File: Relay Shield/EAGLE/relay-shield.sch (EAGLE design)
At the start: 47 parts, among them J1 POWER_JACKSLT, Q1 MPSA42, Q2 MPSA42, Q3 MPSA42, Q4 MPSA42, U1 RELAYPANASONIC-JS, U2 RELAYPANASONIC-JS, U3 RELAYPANASONIC-JS, U4 RELAYPANASONIC-JS, U6 LM2672

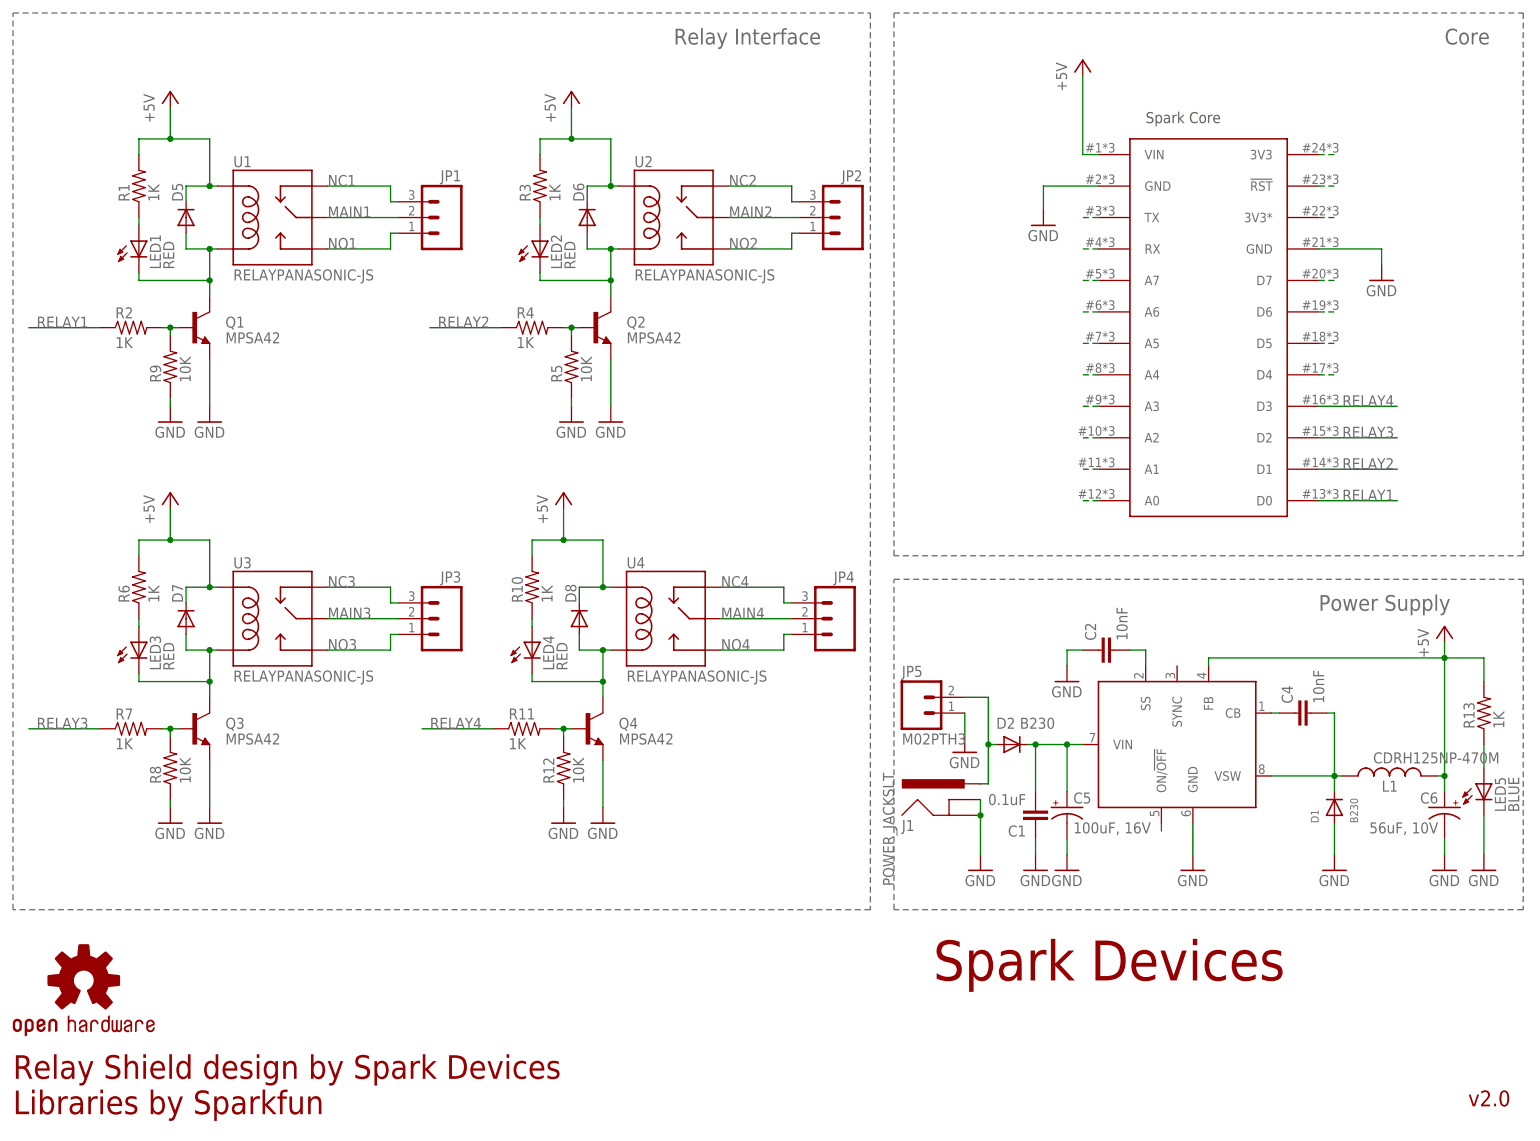
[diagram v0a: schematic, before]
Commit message: updated designators and bom
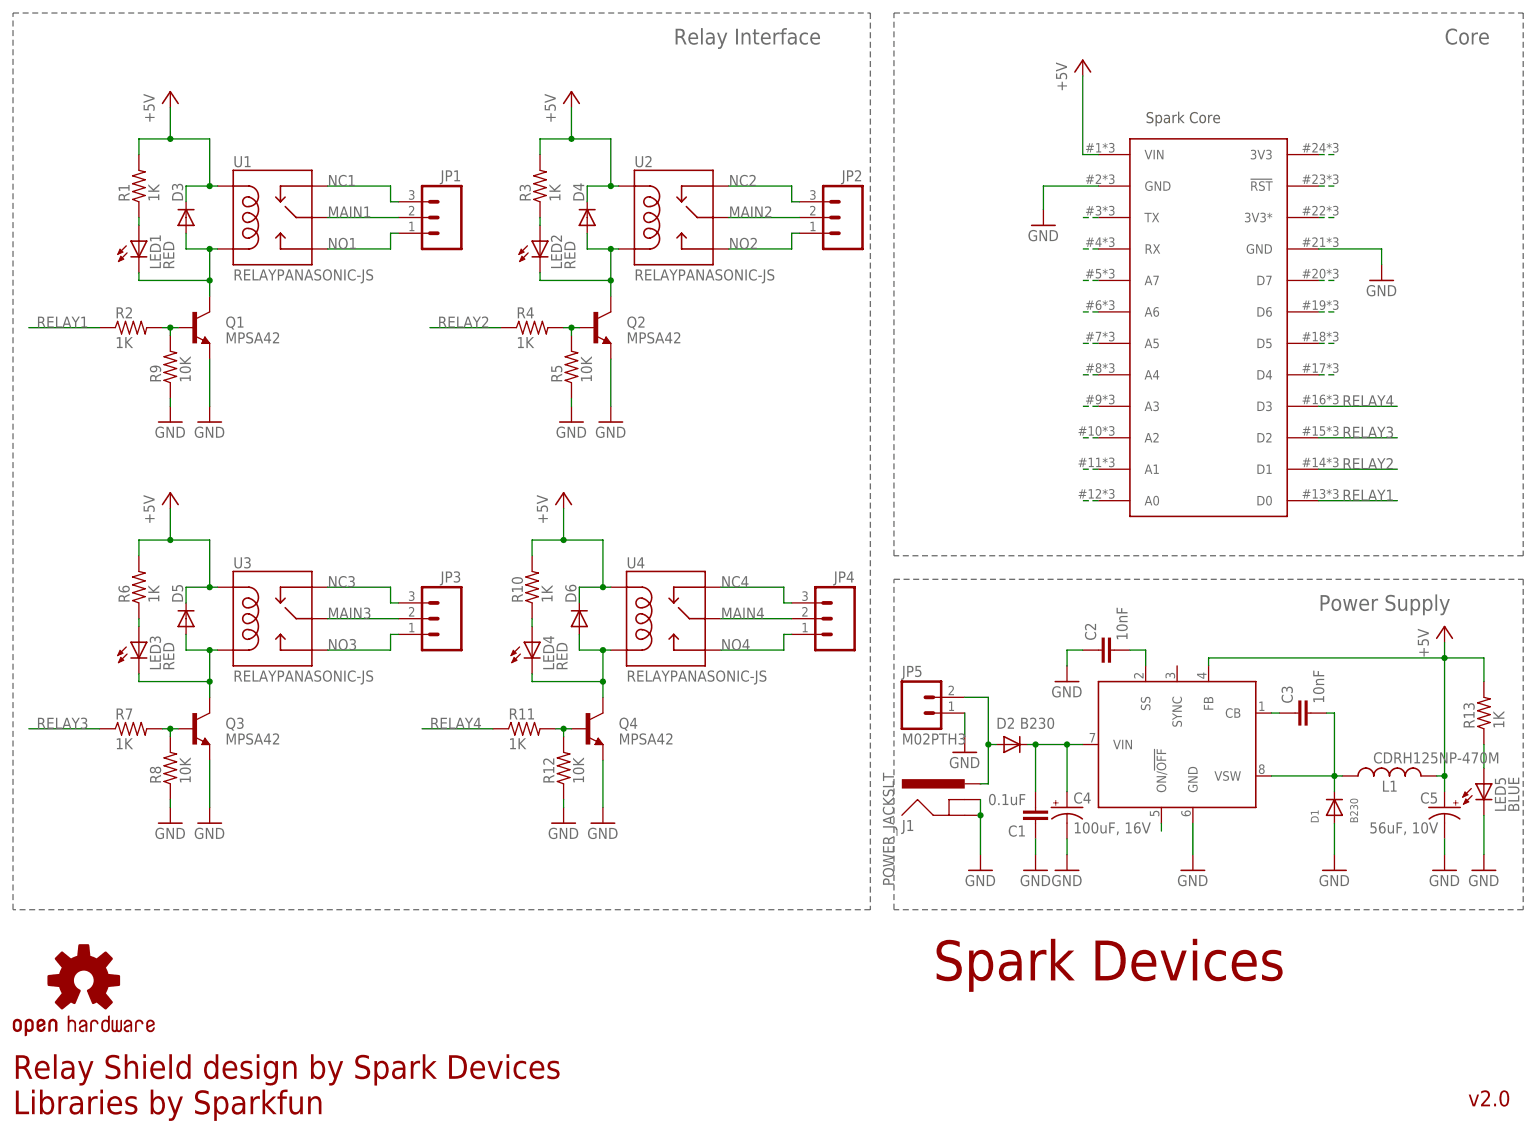
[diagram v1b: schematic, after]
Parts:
- removed C6: 56uF, 10V, SparkFun-Capacitors:CAP_POLD
- removed D7, D8: (no value), diode:DIODE-SOD123
- added C3: 10nF, SparkFun-Capacitors:CAP0603-CAP
- added D3, D4: (no value), diode:DIODE-SOD123
- C4: value 10nF -> 100uF, 16V; device SparkFun-Capacitors:CAP0603-CAP -> SparkFun-Capacitors:CAP_POLD
- C5: value 100uF, 16V -> 56uF, 10V
- renumbered U6 to U5
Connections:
- net +5V: now also C5.+, D3.C, D4.C; no longer C6.+, D7.C, D8.C
- net GND: now also C4.-; no longer C6.-
- net N$1: now also D3.A; no longer D5.A
- net N$11: now also D6.A; no longer D8.A
- net N$14: now also C4.+; no longer C5.+
- net N$33: now also C3.1; no longer C4.1
- net N$34: now also C3.2; no longer C4.2
- net N$5: now also D4.A; no longer D6.A
- net N$8: now also D5.A; no longer D7.A
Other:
- moved on the sheet: C5, D5, D6
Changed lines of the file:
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@@
 <part name="Q3" library="SparkFun-DiscreteSemi" deviceset="TRANSISTOR_NPN" device="MPSA42" value="MPSA42"/>
 <part name="Q4" library="SparkFun-DiscreteSemi" deviceset="TRANSISTOR_NPN" device="MPSA42" value="MPSA42"/>
+<part name="D3" library="diode" deviceset="DIODE-" device="SOD123"/>
+<part name="D4" library="diode" deviceset="DIODE-" device="SOD123"/>
 <part name="D5" library="diode" deviceset="DIODE-" device="SOD123"/>
 <part name="D6" library="diode" deviceset="DIODE-" device="SOD123"/>
-<part name="D7" library="diode" deviceset="DIODE-" device="SOD123"/>
-<part name="D8" library="diode" deviceset="DIODE-" device="SOD123"/>
-<part name="C4" library="SparkFun-Capacitors" deviceset="CAP" device="0603-CAP" value="10nF"/>
-<part name="C5" library="SparkFun-Capacitors" deviceset="CAP_POL" device="D" value="100uF, 16V"/>
-<part name="C6" library="SparkFun-Capacitors" deviceset="CAP_POL" device="D" value="56uF, 10V"/>
+<part name="C3" library="SparkFun-Capacitors" deviceset="CAP" device="0603-CAP" value="10nF"/>
+<part name="C4" library="SparkFun-Capacitors" deviceset="CAP_POL" device="D" value="100uF, 16V"/>
+<part name="C5" library="SparkFun-Capacitors" deviceset="CAP_POL" device="D" value="56uF, 10V"/>
 <part name="D1" library="adafruit" deviceset="DIODE" device="SMA" value="B230"/>
 <part name="D2" library="adafruit" deviceset="DIODE" device="SMA" value="B230"/>
-<part name="U6" library="Spark" deviceset="LM2672" device=""/>
+<part name="U5" library="Spark" deviceset="LM2672" device=""/>
 <part name="GND11" library="supply1" deviceset="GND" device=""/>
 <part name="GND14" library="supply1" deviceset="GND" device=""/>
@@
 <instance part="Q3" gate="G$1" x="31.75" y="67.31"/>
 <instance part="Q4" gate="G$1" x="95.25" y="67.31"/>
-<instance part="D5" gate="G$1" x="30.48" y="149.86" rot="R90"/>
-<instance part="D6" gate="G$1" x="95.25" y="149.86" rot="R90"/>
-<instance part="D7" gate="G$1" x="30.48" y="85.09" rot="R90"/>
-<instance part="D8" gate="G$1" x="93.98" y="85.09" rot="R90"/>
-<instance part="C4" gate="G$1" x="212.09" y="69.85" rot="R90"/>
-<instance part="C5" gate="G$1" x="172.72" y="54.61"/>
-<instance part="C6" gate="G$1" x="233.68" y="54.61" rot="MR0"/>
+<instance part="D3" gate="G$1" x="30.48" y="149.86" rot="R90"/>
+<instance part="D4" gate="G$1" x="95.25" y="149.86" rot="R90"/>
+<instance part="D5" gate="G$1" x="30.48" y="85.09" rot="R90"/>
+<instance part="D6" gate="G$1" x="93.98" y="85.09" rot="R90"/>
+<instance part="C3" gate="G$1" x="212.09" y="69.85" rot="R90"/>
+<instance part="C4" gate="G$1" x="172.72" y="54.61"/>
+<instance part="C5" gate="G$1" x="233.68" y="54.61" rot="MR0"/>
 <instance part="D1" gate="G$1" x="215.9" y="54.61" rot="R90"/>
 <instance part="D2" gate="G$1" x="163.83" y="64.77" smashed="yes">
@@
 <attribute name="VALUE" x="165.1" y="67.31" size="1.778" layer="96"/>
 </instance>
-<instance part="U6" gate="G$1" x="185.42" y="72.39"/>
+<instance part="U5" gate="G$1" x="185.42" y="72.39"/>
 <instance part="GND11" gate="1" x="215.9" y="44.45"/>
 <instance part="GND14" gate="1" x="233.68" y="44.45"/>
@@
 </segment>
 <segment>
-<pinref part="U6" gate="G$1" pin="GND"/>
+<pinref part="U5" gate="G$1" pin="GND"/>
 <pinref part="GND13" gate="1" pin="GND"/>
 <wire x1="193.04" y1="46.99" x2="193.04" y2="52.07" width="0.1524" layer="91"/>
 </segment>
 <segment>
-<pinref part="C5" gate="G$1" pin="-"/>
+<pinref part="C4" gate="G$1" pin="-"/>
 <pinref part="GND12" gate="1" pin="GND"/>
 <wire x1="172.72" y1="46.99" x2="172.72" y2="49.53" width="0.1524" layer="91"/>
@@
 </segment>
 <segment>
-<pinref part="C6" gate="G$1" pin="-"/>
+<pinref part="C5" gate="G$1" pin="-"/>
 <pinref part="GND14" gate="1" pin="GND"/>
 <wire x1="233.68" y1="46.99" x2="233.68" y2="49.53" width="0.1524" layer="91"/>
@@
 <wire x1="27.94" y1="167.64" x2="27.94" y2="162.56" width="0.1524" layer="91"/>
 <junction x="27.94" y="162.56"/>
-<pinref part="D5" gate="G$1" pin="C"/>
+<pinref part="D3" gate="G$1" pin="C"/>
 </segment>
 <segment>
@@
 <wire x1="92.71" y1="167.64" x2="92.71" y2="162.56" width="0.1524" layer="91"/>
 <junction x="92.71" y="162.56"/>
-<pinref part="D6" gate="G$1" pin="C"/>
+<pinref part="D4" gate="G$1" pin="C"/>
 </segment>
 <segment>
@@
 <wire x1="27.94" y1="102.87" x2="27.94" y2="97.79" width="0.1524" layer="91"/>
 <junction x="27.94" y="97.79"/>
-<pinref part="D7" gate="G$1" pin="C"/>
+<pinref part="D5" gate="G$1" pin="C"/>
 </segment>
 <segment>
@@
 <wire x1="91.44" y1="102.87" x2="91.44" y2="97.79" width="0.1524" layer="91"/>
 <junction x="91.44" y="97.79"/>
-<pinref part="D8" gate="G$1" pin="C"/>
-</segment>
-<segment>
-<pinref part="U6" gate="G$1" pin="FB"/>
+<pinref part="D6" gate="G$1" pin="C"/>
+</segment>
+<segment>
+<pinref part="U5" gate="G$1" pin="FB"/>
 <wire x1="195.58" y1="77.47" x2="195.58" y2="78.74" width="0.1524" layer="91"/>
-<pinref part="C6" gate="G$1" pin="+"/>
+<pinref part="C5" gate="G$1" pin="+"/>
 <wire x1="195.58" y1="78.74" x2="233.68" y2="78.74" width="0.1524" layer="91"/>
 <wire x1="233.68" y1="78.74" x2="233.68" y2="59.69" width="0.1524" layer="91"/>
@@
 <junction x="34.29" y="139.7"/>
 <pinref part="Q1" gate="G$1" pin="C"/>
-<pinref part="D5" gate="G$1" pin="A"/>
+<pinref part="D3" gate="G$1" pin="A"/>
 </segment>
 </net>
@@
 <junction x="99.06" y="139.7"/>
 <pinref part="Q2" gate="G$1" pin="C"/>
-<pinref part="D6" gate="G$1" pin="A"/>
+<pinref part="D4" gate="G$1" pin="A"/>
 </segment>
 </net>
@@
 <junction x="34.29" y="74.93"/>
 <pinref part="Q3" gate="G$1" pin="C"/>
-<pinref part="D7" gate="G$1" pin="A"/>
+<pinref part="D5" gate="G$1" pin="A"/>
 </segment>
 </net>
@@
 <junction x="97.79" y="74.93"/>
 <pinref part="Q4" gate="G$1" pin="C"/>
-<pinref part="D8" gate="G$1" pin="A"/>
+<pinref part="D6" gate="G$1" pin="A"/>
 </segment>
 </net>
@@
 <net name="N$14" class="0">
 <segment>
-<pinref part="C5" gate="G$1" pin="+"/>
-<pinref part="U6" gate="G$1" pin="VIN"/>
+<pinref part="C4" gate="G$1" pin="+"/>
+<pinref part="U5" gate="G$1" pin="VIN"/>
 <wire x1="172.72" y1="57.15" x2="172.72" y2="64.77" width="0.1524" layer="91"/>
 <wire x1="172.72" y1="64.77" x2="175.26" y2="64.77" width="0.1524" layer="91"/>
@@
 <net name="N$33" class="0">
 <segment>
-<pinref part="U6" gate="G$1" pin="CB"/>
-<pinref part="C4" gate="G$1" pin="1"/>
+<pinref part="U5" gate="G$1" pin="CB"/>
+<pinref part="C3" gate="G$1" pin="1"/>
 <wire x1="207.01" y1="69.85" x2="205.74" y2="69.85" width="0.1524" layer="91"/>
 </segment>
@@
 <net name="N$34" class="0">
 <segment>
-<pinref part="U6" gate="G$1" pin="VSW"/>
+<pinref part="U5" gate="G$1" pin="VSW"/>
 <pinref part="D1" gate="G$1" pin="C"/>
 <wire x1="205.74" y1="59.69" x2="215.9" y2="59.69" width="0.1524" layer="91"/>
@@
 <wire x1="217.17" y1="59.69" x2="215.9" y2="59.69" width="0.1524" layer="91"/>
 <junction x="215.9" y="59.69"/>
-<pinref part="C4" gate="G$1" pin="2"/>
+<pinref part="C3" gate="G$1" pin="2"/>
 <wire x1="214.63" y1="69.85" x2="215.9" y2="69.85" width="0.1524" layer="91"/>
 <wire x1="215.9" y1="69.85" x2="215.9" y2="59.69" width="0.1524" layer="91"/>
@@
 <net name="N$35" class="0">
 <segment>
-<pinref part="U6" gate="G$1" pin="ON/!OFF"/>
+<pinref part="U5" gate="G$1" pin="ON/!OFF"/>
 <wire x1="187.96" y1="52.07" x2="187.96" y2="50.8" width="0.1524" layer="91"/>
 </segment>
@@
 <segment>
 <pinref part="C2" gate="G$1" pin="2"/>
-<pinref part="U6" gate="G$1" pin="SS"/>
+<pinref part="U5" gate="G$1" pin="SS"/>
 <wire x1="182.88" y1="80.01" x2="185.42" y2="80.01" width="0.1524" layer="91"/>
 <wire x1="185.42" y1="80.01" x2="185.42" y2="77.47" width="0.1524" layer="91"/>
